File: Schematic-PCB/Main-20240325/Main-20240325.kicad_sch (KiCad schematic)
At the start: 104 parts, among them J1 Conn_01x10_Pin, J2 Conn_01x03_Pin, J3 Conn_01x15_Pin, J4 Conn_02x05_Odd_Even, J5 Conn_01x04_Pin, U1 DEV-16771, U10 TSSP58038, U11 TSSP58038, U12 TSSP58038, U13 TSSP58038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

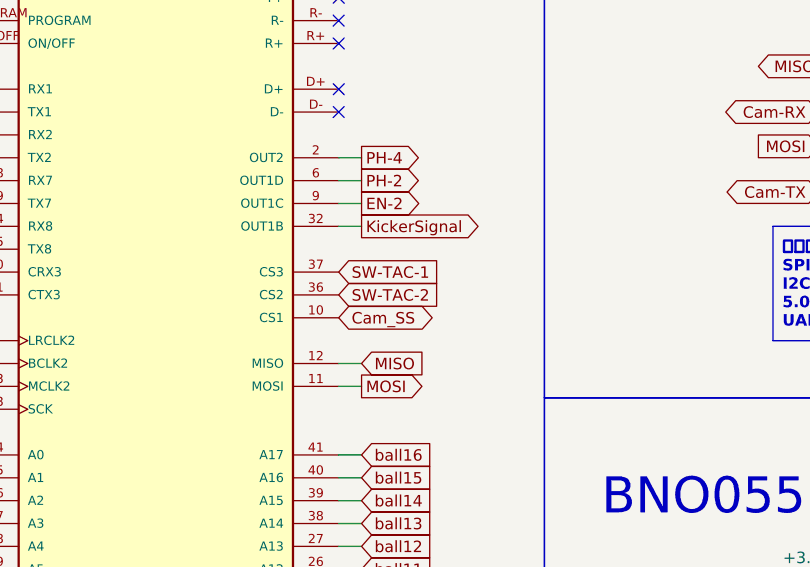
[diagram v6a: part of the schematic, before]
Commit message: ラインセンサ基板とメイン基板のDR進めたよ
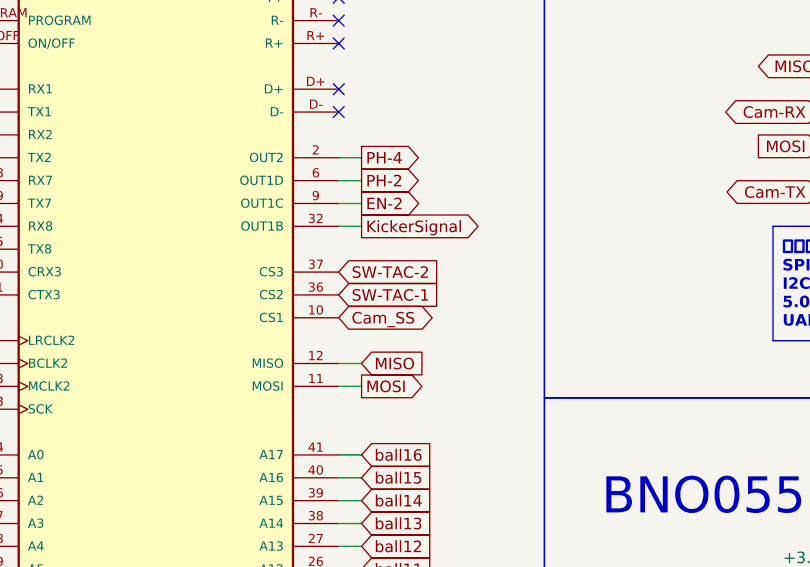
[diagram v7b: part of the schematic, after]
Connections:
- net SW-TAC-1: now also U1.36 (CS2); no longer U1.37 (CS3)
- net SW-TAC-2: now also U1.37 (CS3); no longer U1.36 (CS2)
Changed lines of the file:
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@@
 	(global_label "SW-TAC-1"
 		(shape input)
+		(at 74.93 81.28 0)
+		(fields_autoplaced yes)
+		(effects
+			(font
+				(size 1.27 1.27)
+			)
+			(justify left)
+		)
+		(property "Intersheetrefs" "${INTERSHEET_REFS}"
+			(at 86.9996 81.28 0)
+			(effects
+				(font
+					(size 1.27 1.27)
+				)
+				(justify left)
+				(hide yes)
+			)
+		)
+	)
+	(global_label "PH-1"
+		(shape output)
+		(at 31.75 68.58 180)
+		(fields_autoplaced yes)
+		(effects
+			(font
+				(size 1.27 1.27)
+			)
+			(justify right)
+		)
+		(property "Intersheetrefs" "${INTERSHEET_REFS}"
+			(at 23.3824 68.58 0)
+			(effects
+				(font
+					(size 1.27 1.27)
+				)
+				(justify right)
+				(hide yes)
+			)
+		)
+	)
+	(global_label "ball14"
+		(shape output)
+		(at 193.04 294.64 0)
+		(fields_autoplaced yes)
+		(effects
+			(font
+				(size 1.27 1.27)
+			)
+			(justify left)
+		)
+		(property "Intersheetrefs" "${INTERSHEET_REFS}"
+			(at 201.7261 294.64 0)
+			(effects
+				(font
+					(size 1.27 1.27)
+				)
+				(justify left)
+				(hide yes)
+			)
+		)
+	)
+	(global_label "PH-3"
+		(shape input)
+		(at 36.83 363.22 0)
+		(fields_autoplaced yes)
+		(effects
+			(font
+				(size 1.27 1.27)
+			)
+			(justify left)
+		)
+		(property "Intersheetrefs" "${INTERSHEET_REFS}"
+			(at 45.1976 363.22 0)
+			(effects
+				(font
+					(size 1.27 1.27)
+				)
+				(justify left)
+				(hide yes)
+			)
+		)
+	)
+	(global_label "SW-TAC-4"
+		(shape input)
+		(at 31.75 78.74 180)
+		(fields_autoplaced yes)
+		(effects
+			(font
+				(size 1.27 1.27)
+			)
+			(justify right)
+		)
+		(property "Intersheetrefs" "${INTERSHEET_REFS}"
+			(at 19.6804 78.74 0)
+			(effects
+				(font
+					(size 1.27 1.27)
+				)
+				(justify right)
+				(hide yes)
+			)
+		)
+	)
+	(global_label "BUZZER"
+		(shape input)
+		(at 36.83 314.96 0)
+		(fields_autoplaced yes)
+		(effects
+			(font
+				(size 1.27 1.27)
+			)
+			(justify left)
+		)
+		(property "Intersheetrefs" "${INTERSHEET_REFS}"
+			(at 47.2537 314.96 0)
+			(effects
+				(font
+					(size 1.27 1.27)
+				)
+				(justify left)
+				(hide yes)
+			)
+		)
+	)
+	(global_label "ball04"
+		(shape output)
+		(at 144.78 248.92 0)
+		(fields_autoplaced yes)
+		(effects
+			(font
+				(size 1.27 1.27)
+			)
+			(justify left)
+		)
+		(property "Intersheetrefs" "${INTERSHEET_REFS}"
+			(at 153.4661 248.92 0)
+			(effects
+				(font
+					(size 1.27 1.27)
+				)
+				(justify left)
+				(hide yes)
+			)
+		)
+	)
+	(global_label "ball16"
+		(shape output)
+		(at 193.04 340.36 0)
+		(fields_autoplaced yes)
+		(effects
+			(font
+				(size 1.27 1.27)
+			)
+			(justify left)
+		)
+		(property "Intersheetrefs" "${INTERSHEET_REFS}"
+			(at 201.7261 340.36 0)
+			(effects
+				(font
+					(size 1.27 1.27)
+				)
+				(justify left)
+				(hide yes)
+			)
+		)
+	)
+	(global_label "PH-2"
+		(shape output)
+		(at 77.47 68.58 0)
+		(fields_autoplaced yes)
+		(effects
+			(font
+				(size 1.27 1.27)
+			)
+			(justify left)
+		)
+		(property "Intersheetrefs" "${INTERSHEET_REFS}"
+			(at 85.8376 68.58 0)
+			(effects
+				(font
+					(size 1.27 1.27)
+				)
+				(justify left)
+				(hide yes)
+			)
+		)
+	)
+	(global_label "SW-TAC-2"
+		(shape input)
 		(at 74.93 78.74 0)
 		(fields_autoplaced yes)
@@
 			(effects
 				(font
-					(size 1.27 1.27)
-				)
-				(justify left)
-				(hide yes)
-			)
-		)
-	)
-	(global_label "PH-1"
-		(shape output)
-		(at 31.75 68.58 180)
-		(fields_autoplaced yes)
-		(effects
-			(font
-				(size 1.27 1.27)
-			)
-			(justify right)
-		)
-		(property "Intersheetrefs" "${INTERSHEET_REFS}"
-			(at 23.3824 68.58 0)
-			(effects
-				(font
-					(size 1.27 1.27)
-				)
-				(justify right)
-				(hide yes)
-			)
-		)
-	)
-	(global_label "ball14"
-		(shape output)
-		(at 193.04 294.64 0)
-		(fields_autoplaced yes)
-		(effects
-			(font
-				(size 1.27 1.27)
-			)
-			(justify left)
-		)
-		(property "Intersheetrefs" "${INTERSHEET_REFS}"
-			(at 201.7261 294.64 0)
-			(effects
-				(font
-					(size 1.27 1.27)
-				)
-				(justify left)
-				(hide yes)
-			)
-		)
-	)
-	(global_label "PH-3"
-		(shape input)
-		(at 36.83 363.22 0)
-		(fields_autoplaced yes)
-		(effects
-			(font
-				(size 1.27 1.27)
-			)
-			(justify left)
-		)
-		(property "Intersheetrefs" "${INTERSHEET_REFS}"
-			(at 45.1976 363.22 0)
-			(effects
-				(font
-					(size 1.27 1.27)
-				)
-				(justify left)
-				(hide yes)
-			)
-		)
-	)
-	(global_label "SW-TAC-4"
-		(shape input)
-		(at 31.75 78.74 180)
-		(fields_autoplaced yes)
-		(effects
-			(font
-				(size 1.27 1.27)
-			)
-			(justify right)
-		)
-		(property "Intersheetrefs" "${INTERSHEET_REFS}"
-			(at 19.6804 78.74 0)
-			(effects
-				(font
-					(size 1.27 1.27)
-				)
-				(justify right)
-				(hide yes)
-			)
-		)
-	)
-	(global_label "BUZZER"
-		(shape input)
-		(at 36.83 314.96 0)
-		(fields_autoplaced yes)
-		(effects
-			(font
-				(size 1.27 1.27)
-			)
-			(justify left)
-		)
-		(property "Intersheetrefs" "${INTERSHEET_REFS}"
-			(at 47.2537 314.96 0)
-			(effects
-				(font
-					(size 1.27 1.27)
-				)
-				(justify left)
-				(hide yes)
-			)
-		)
-	)
-	(global_label "ball04"
-		(shape output)
-		(at 144.78 248.92 0)
-		(fields_autoplaced yes)
-		(effects
-			(font
-				(size 1.27 1.27)
-			)
-			(justify left)
-		)
-		(property "Intersheetrefs" "${INTERSHEET_REFS}"
-			(at 153.4661 248.92 0)
-			(effects
-				(font
-					(size 1.27 1.27)
-				)
-				(justify left)
-				(hide yes)
-			)
-		)
-	)
-	(global_label "ball16"
-		(shape output)
-		(at 193.04 340.36 0)
-		(fields_autoplaced yes)
-		(effects
-			(font
-				(size 1.27 1.27)
-			)
-			(justify left)
-		)
-		(property "Intersheetrefs" "${INTERSHEET_REFS}"
-			(at 201.7261 340.36 0)
-			(effects
-				(font
-					(size 1.27 1.27)
-				)
-				(justify left)
-				(hide yes)
-			)
-		)
-	)
-	(global_label "PH-2"
-		(shape output)
-		(at 77.47 68.58 0)
-		(fields_autoplaced yes)
-		(effects
-			(font
-				(size 1.27 1.27)
-			)
-			(justify left)
-		)
-		(property "Intersheetrefs" "${INTERSHEET_REFS}"
-			(at 85.8376 68.58 0)
-			(effects
-				(font
-					(size 1.27 1.27)
-				)
-				(justify left)
-				(hide yes)
-			)
-		)
-	)
-	(global_label "SW-TAC-2"
-		(shape input)
-		(at 74.93 81.28 0)
-		(fields_autoplaced yes)
-		(effects
-			(font
-				(size 1.27 1.27)
-			)
-			(justify left)
-		)
-		(property "Intersheetrefs" "${INTERSHEET_REFS}"
-			(at 86.9996 81.28 0)
-			(effects
-				(font

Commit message: メイン基板のDR完了
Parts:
- J3: footprint @2024-MD:1.0K-FX-15PWB -> @2024TOINIOT2-MD:1.0K-FX-15PWB
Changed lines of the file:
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@@
 			)
 		)
-		(property "Footprint" "@2024-MD:1.0K-FX-15PWB"
+		(property "Footprint" "@2024TOINIOT2-MD:1.0K-FX-15PWB"
 			(at 29.21 368.3 0)
 			(effects
